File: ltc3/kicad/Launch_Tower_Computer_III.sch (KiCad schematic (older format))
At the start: 0 parts

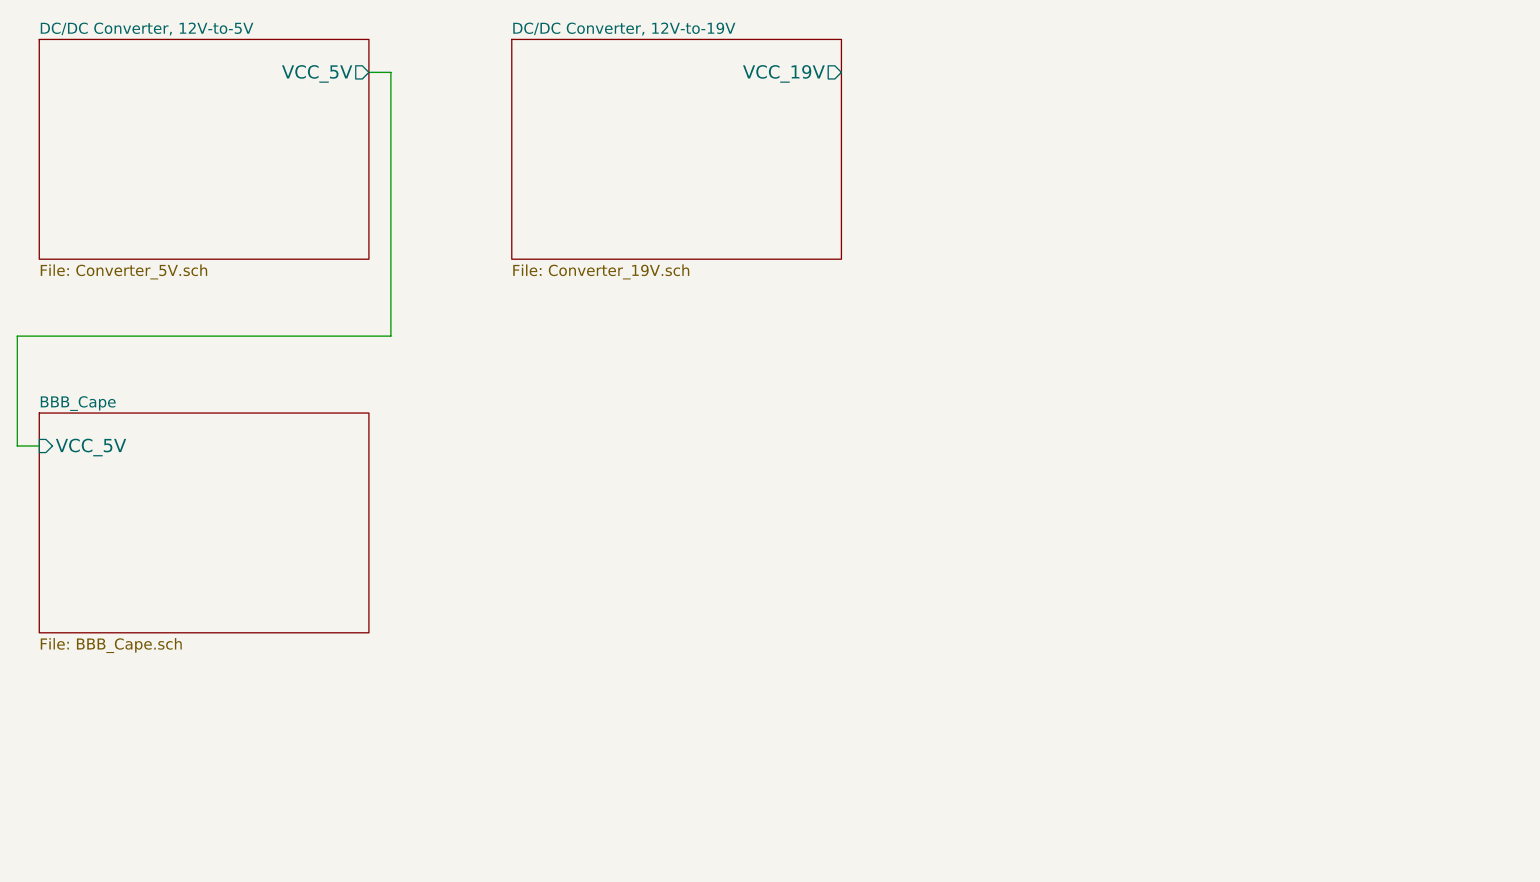
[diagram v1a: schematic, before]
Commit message: More work on LTC3 schematic. 1. Created placeholder "power in" schematic. 2. First cut at external trigger schematic (MOSTFETs and mechanical    relays).
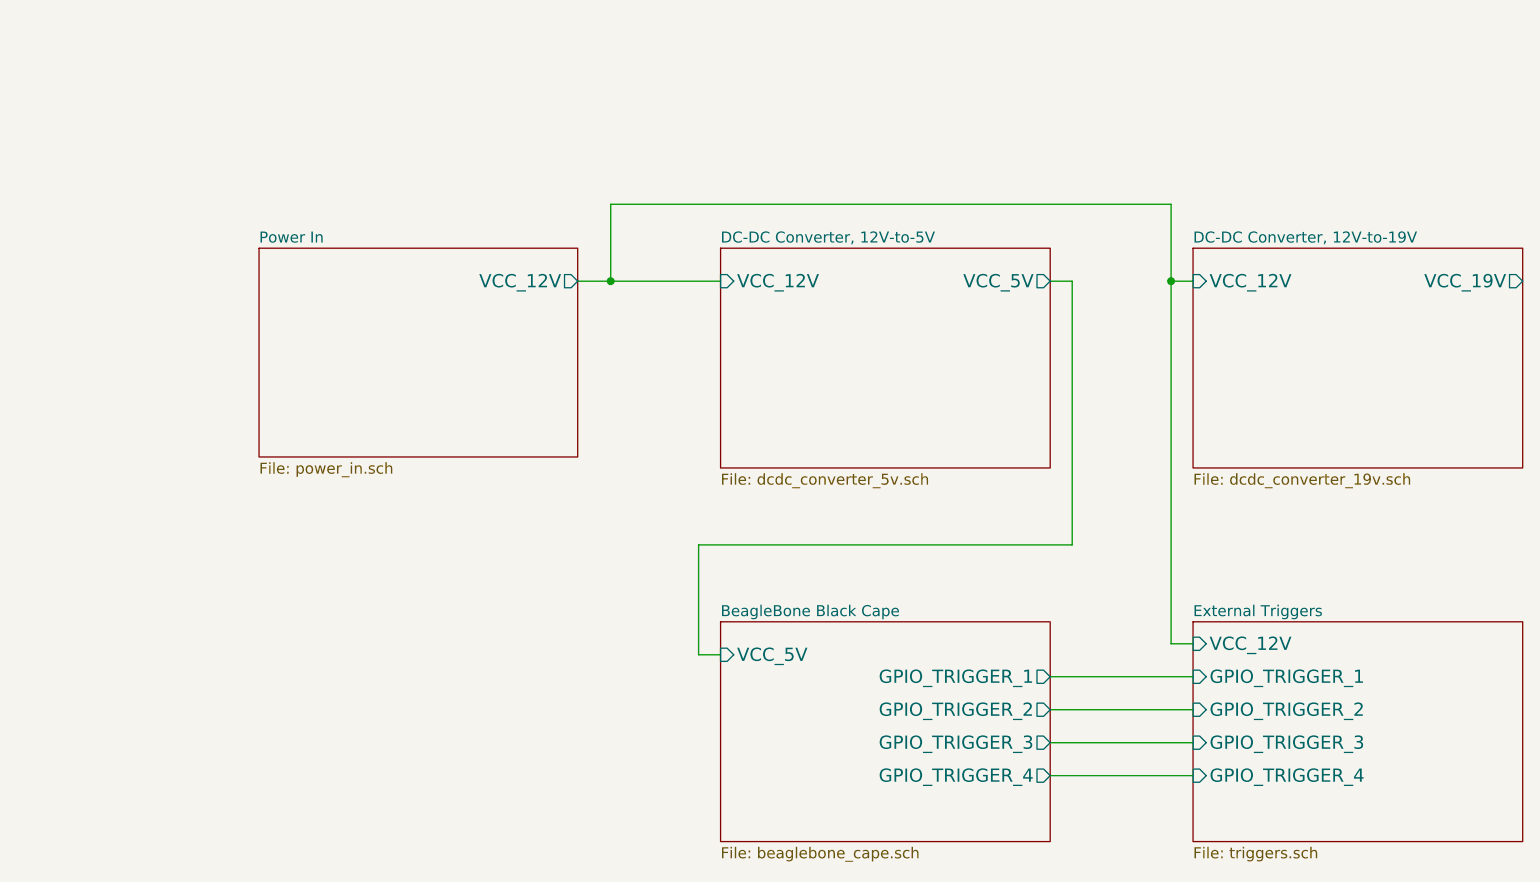
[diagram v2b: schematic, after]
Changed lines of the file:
@@
 LIBS:LTC299x
 LIBS:memory_devices
+LIBS:switches
 LIBS:Launch_Tower_Computer_III-cache
 EELAYER 27 0
@@
 $Descr USLetter 11000 8500
 encoding utf-8
-Sheet 1 4
+Sheet 1 6
 Title "Launch Tower Computer III (LTC3)"
-Date "16 mar 2015"
+Date "2 apr 2015"
 Rev "1"
 Comp "Portland State Aerospace Society <http://psas.pdx.edu/>"
@@
 $EndDescr
 $Sheet
-S 900  2600 1500 1000
-U 55051BA8
-F0 "BBB_Cape" 50
-F1 "BBB_Cape.sch" 50
-F2 "VCC_5V" I L 900 2750 60
+S 1900 1850 1450 950
+U 551C8EE6
+F0 "Power In" 50
+F1 "power_in.sch" 50
+F2 "VCC_12V" O R 3350 2000 60
 $EndSheet
 $Sheet
-S 900  900  1500 1000
+S 4000 1850 1500 1000
 U 550535FB
-F0 "DC/DC Converter, 12V-to-5V" 50
-F1 "Converter_5V.sch" 50
-F2 "VCC_5V" O R 2400 1050 60
+F0 "DC-DC Converter, 12V-to-5V" 50
+F1 "dcdc_converter_5v.sch" 50
+F2 "VCC_5V" O R 5500 2000 60
+F3 "VCC_12V" I L 4000 2000 60
 $EndSheet
 $Sheet
-S 3050 900  1500 1000
+S 6150 1850 1500 1000
 U 55053600
-F0 "DC/DC Converter, 12V-to-19V" 50
-F1 "Converter_19V.sch" 50
-F2 "VCC_19V" O R 4550 1050 60
+F0 "DC-DC Converter, 12V-to-19V" 50
+F1 "dcdc_converter_19v.sch" 50
+F2 "VCC_19V" O R 7650 2000 60
+F3 "VCC_12V" I L 6150 2000 60
+$EndSheet
+$Sheet
+S 4000 3550 1500 1000
+U 55051BA8
+F0 "BeagleBone Black Cape" 50
+F1 "beaglebone_cape.sch" 50
+F2 "VCC_5V" I L 4000 3700 60
+F3 "GPIO_TRIGGER_1" O R 5500 3800 60
+F4 "GPIO_TRIGGER_2" O R 5500 3950 60
+F5 "GPIO_TRIGGER_3" O R 5500 4100 60
+F6 "GPIO_TRIGGER_4" O R 5500 4250 60
 $EndSheet
 Wire Wire Line
-	2400 1050 2500 1050
+	5500 2000 5600 2000
 Wire Wire Line
-	2500 1050 2500 2250
+	5600 2000 5600 3200
 Wire Wire Line
-	2500 2250 800  2250
+	5600 3200 3900 3200
 Wire Wire Line
-	800  2250 800  2750
+	3900 3200 3900 3700
 Wire Wire Line
-	800  2750 900  2750
+	3900 3700 4000 3700
+$Sheet
+S 6150 3550 1500 1000
+U 551C79BE
+F0 "External Triggers" 50
+F1 "triggers.sch" 50
+F2 "GPIO_TRIGGER_1" I L 6150 3800 60
+F3 "GPIO_TRIGGER_2" I L 6150 3950 60
+F4 "GPIO_TRIGGER_3" I L 6150 4100 60
+F5 "GPIO_TRIGGER_4" I L 6150 4250 60
+F6 "VCC_12V" I L 6150 3650 60
+$EndSheet
+Wire Wire Line
+	5500 3800 6150 3800
+Wire Wire Line
+	5500 3950 6150 3950
+Wire Wire Line
+	6150 4100 5500 4100
+Wire Wire Line
+	5500 4250 6150 4250
+Wire Wire Line
+	3350 2000 4000 2000
+Wire Wire Line
+	3500 2000 3500 1650
+Wire Wire Line
+	3500 1650 6050 1650
+Wire Wire Line
+	6050 1650 6050 3650
+Wire Wire Line
+	6050 2000 6150 2000
+Connection ~ 3500 2000
+Wire Wire Line
+	6050 3650 6150 3650
+Connection ~ 6050 2000
 $EndSCHEMATC

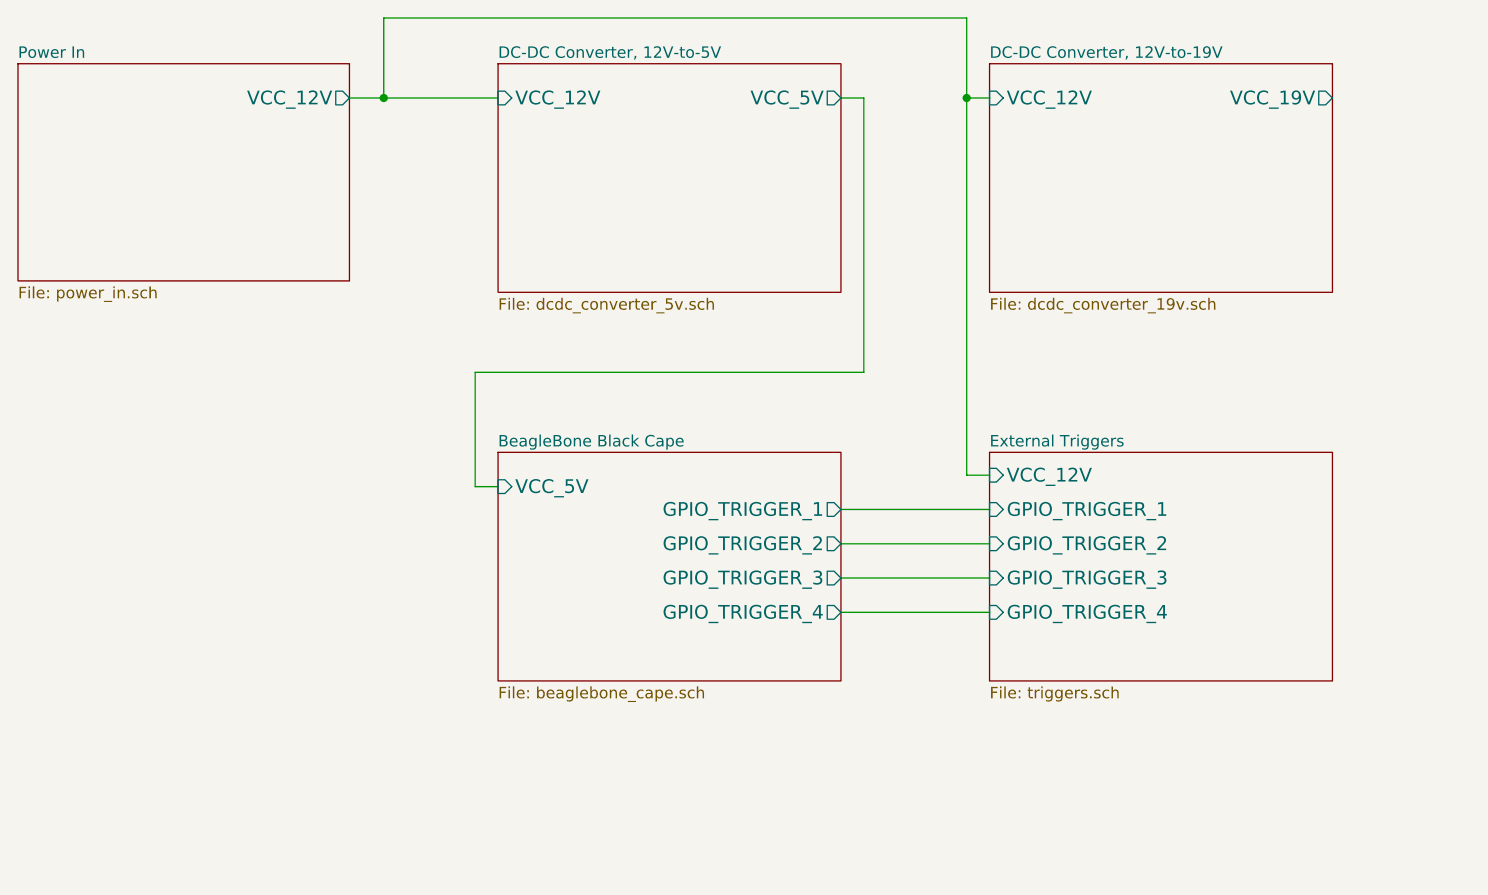
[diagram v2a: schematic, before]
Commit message: Fixed mistakes in triggers schematic; misc. clean-up.
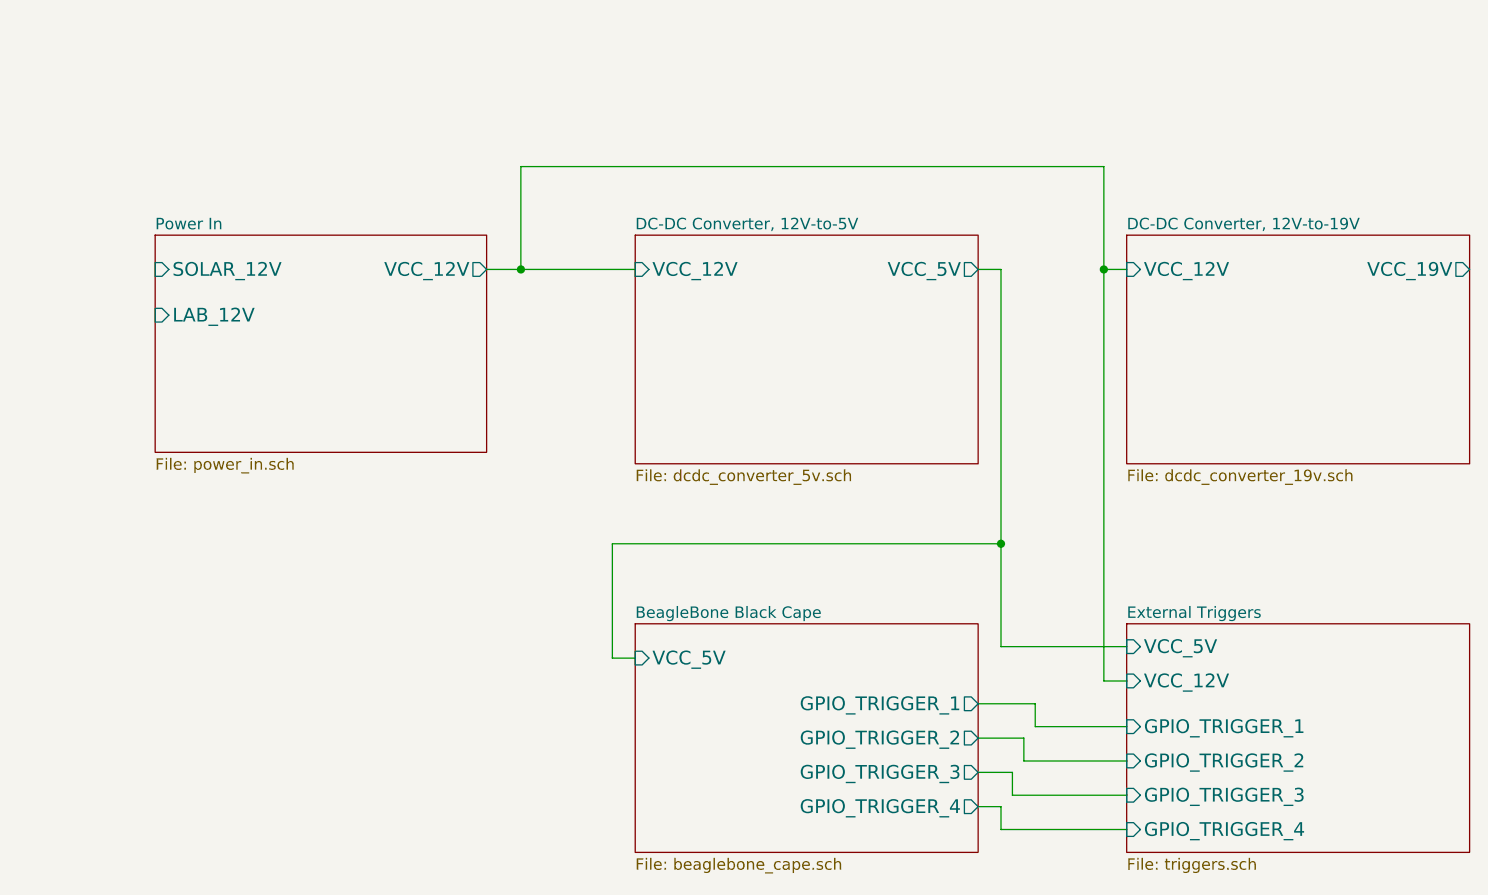
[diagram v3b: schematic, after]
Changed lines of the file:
@@
 $EndDescr
 $Sheet
-S 1900 1850 1450 950
+S 2500 2600 1450 950
 U 551C8EE6
 F0 "Power In" 50
 F1 "power_in.sch" 50
-F2 "VCC_12V" O R 3350 2000 60
+F2 "VCC_12V" O R 3950 2750 60
+F3 "SOLAR_12V" I L 2500 2750 60
+F4 "LAB_12V" I L 2500 2950 60
 $EndSheet
 $Sheet
-S 4000 1850 1500 1000
+S 4600 2600 1500 1000
 U 550535FB
 F0 "DC-DC Converter, 12V-to-5V" 50
 F1 "dcdc_converter_5v.sch" 50
-F2 "VCC_5V" O R 5500 2000 60
-F3 "VCC_12V" I L 4000 2000 60
+F2 "VCC_5V" O R 6100 2750 60
+F3 "VCC_12V" I L 4600 2750 60
 $EndSheet
 $Sheet
-S 6150 1850 1500 1000
+S 6750 2600 1500 1000
 U 55053600
 F0 "DC-DC Converter, 12V-to-19V" 50
 F1 "dcdc_converter_19v.sch" 50
-F2 "VCC_19V" O R 7650 2000 60
-F3 "VCC_12V" I L 6150 2000 60
+F2 "VCC_19V" O R 8250 2750 60
+F3 "VCC_12V" I L 6750 2750 60
 $EndSheet
 $Sheet
-S 4000 3550 1500 1000
+S 4600 4300 1500 1000
 U 55051BA8
 F0 "BeagleBone Black Cape" 50
 F1 "beaglebone_cape.sch" 50
-F2 "VCC_5V" I L 4000 3700 60
-F3 "GPIO_TRIGGER_1" O R 5500 3800 60
-F4 "GPIO_TRIGGER_2" O R 5500 3950 60
-F5 "GPIO_TRIGGER_3" O R 5500 4100 60
-F6 "GPIO_TRIGGER_4" O R 5500 4250 60
+F2 "VCC_5V" I L 4600 4450 60
+F3 "GPIO_TRIGGER_1" O R 6100 4650 60
+F4 "GPIO_TRIGGER_2" O R 6100 4800 60
+F5 "GPIO_TRIGGER_3" O R 6100 4950 60
+F6 "GPIO_TRIGGER_4" O R 6100 5100 60
 $EndSheet
 Wire Wire Line
-	5500 2000 5600 2000
+	6100 2750 6200 2750
 Wire Wire Line
-	5600 2000 5600 3200
+	6200 2750 6200 4400
 Wire Wire Line
-	5600 3200 3900 3200
+	6200 3950 4500 3950
 Wire Wire Line
-	3900 3200 3900 3700
+	4500 3950 4500 4450
 Wire Wire Line
-	3900 3700 4000 3700
+	4500 4450 4600 4450
+Wire Wire Line
+	3950 2750 4600 2750
+Wire Wire Line
+	6650 2750 6750 2750
+Wire Wire Line
+	6200 4400 6750 4400
 $Sheet
-S 6150 3550 1500 1000
+S 6750 4300 1500 1000
 U 551C79BE
 F0 "External Triggers" 50
 F1 "triggers.sch" 50
-F2 "GPIO_TRIGGER_1" I L 6150 3800 60
-F3 "GPIO_TRIGGER_2" I L 6150 3950 60
-F4 "GPIO_TRIGGER_3" I L 6150 4100 60
-F5 "GPIO_TRIGGER_4" I L 6150 4250 60
-F6 "VCC_12V" I L 6150 3650 60
+F2 "GPIO_TRIGGER_1" I L 6750 4750 60
+F3 "GPIO_TRIGGER_2" I L 6750 4900 60
+F4 "GPIO_TRIGGER_3" I L 6750 5050 60
+F5 "GPIO_TRIGGER_4" I L 6750 5200 60
+F6 "VCC_12V" I L 6750 4550 60
+F7 "VCC_5V" I L 6750 4400 60
 $EndSheet
 Wire Wire Line
-	5500 3800 6150 3800
+	6650 4550 6750 4550
+Connection ~ 6200 3950
 Wire Wire Line
-	5500 3950 6150 3950
+	4100 2750 4100 2300
 Wire Wire Line
-	6150 4100 5500 4100
+	4100 2300 6650 2300
 Wire Wire Line
-	5500 4250 6150 4250
+	6650 2300 6650 4550
+Connection ~ 4100 2750
+Connection ~ 6650 2750
 Wire Wire Line
-	3350 2000 4000 2000
+	6100 4650 6350 4650
 Wire Wire Line
-	3500 2000 3500 1650
+	6350 4650 6350 4750
 Wire Wire Line
-	3500 1650 6050 1650
+	6350 4750 6750 4750
 Wire Wire Line
-	6050 1650 6050 3650
+	6100 4800 6300 4800
 Wire Wire Line
-	6050 2000 6150 2000
-Connection ~ 3500 2000
+	6300 4800 6300 4900
 Wire Wire Line
-	6050 3650 6150 3650
-Connection ~ 6050 2000
+	6300 4900 6750 4900
+Wire Wire Line
+	6100 4950 6250 4950
+Wire Wire Line
+	6250 4950 6250 5050
+Wire Wire Line
+	6250 5050 6750 5050
+Wire Wire Line
+	6100 5100 6200 5100
+Wire Wire Line
+	6200 5100 6200 5200
+Wire Wire Line
+	6200 5200 6750 5200
 $EndSCHEMATC
